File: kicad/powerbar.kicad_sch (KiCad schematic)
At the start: 24 parts, among them J31 Float 1, J32 Float 2, J33 Power bar 1, J34 Power bar 2, U10 PCA9685PW

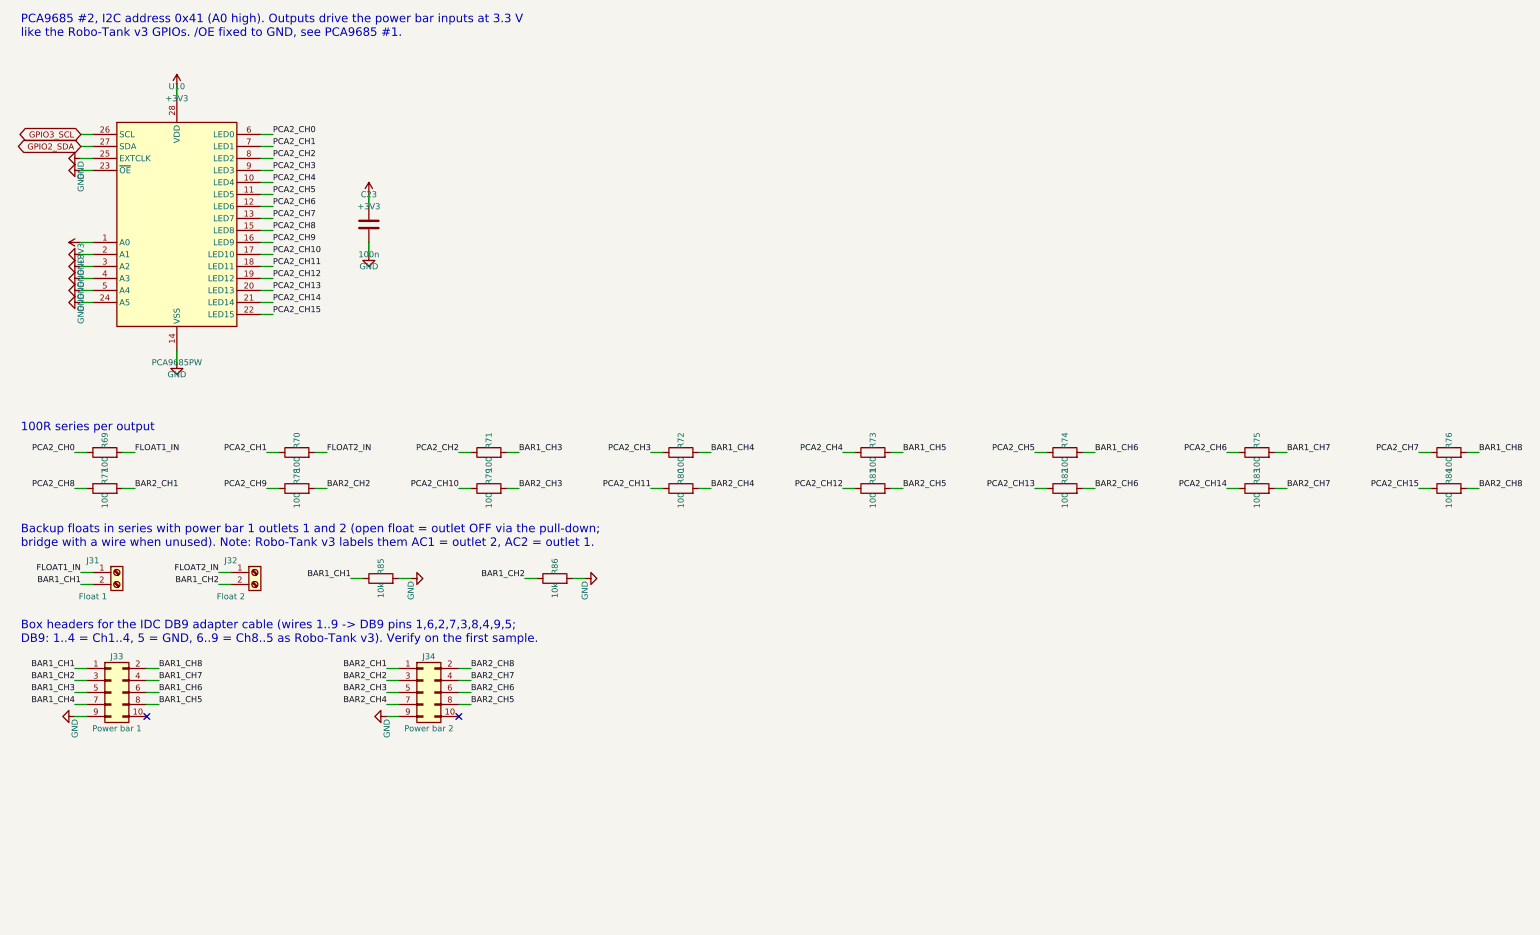
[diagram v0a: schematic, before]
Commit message: kicad: v2 space measures - feeder on power bar header, resistor arrays, 0603, TSSOP buffers
Feeder port dropped: power bar header pin 10 = +3V3_EXT (own AMS1117), any PCA #2 channel as signal; 30 series resistors as 8x 4x0603 arrays; new passives 0603; new 74HCT244 in TSSOP-20; flat parts may use the Pi zone, connectors anywhere else. ERC 0, DRC copper 0, parity 0.

Co-Authored-By: Claude Opus 5.5 <noreply@anthropic.com>
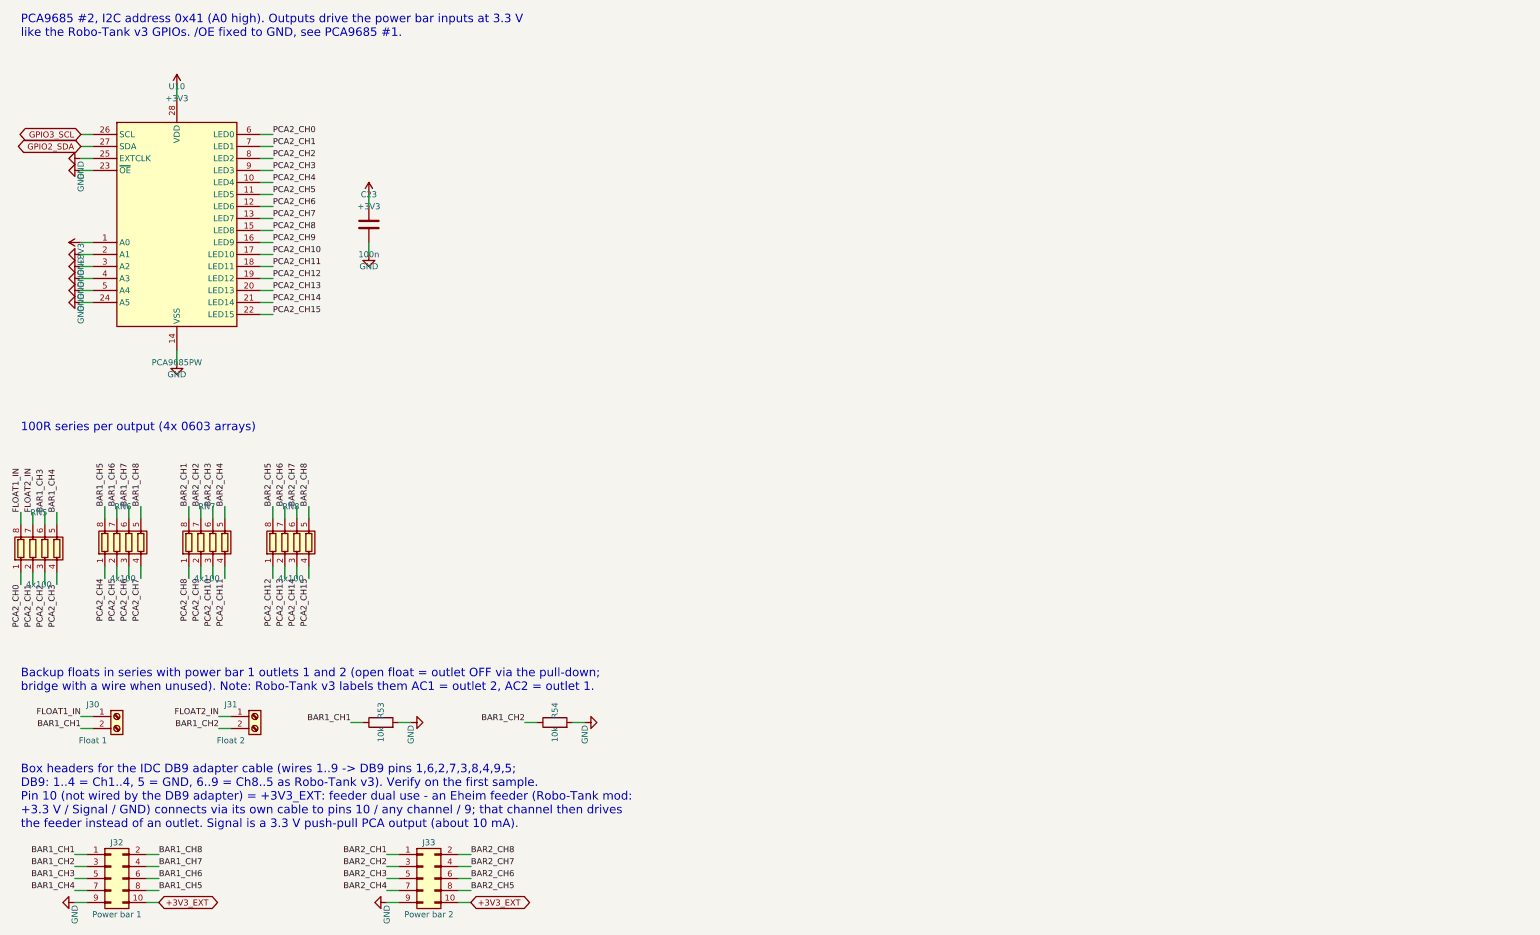
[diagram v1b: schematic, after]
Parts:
- removed J32: Float 2, aquaPCB:TerminalBlock_Kangnex_WJ250B-3.5-02P_P3.50mm_Staggered, symbol Connector:Screw_Terminal_01x02
- removed J34: Power bar 2, Connector_IDC:IDC-Header_2x05_P2.54mm_Vertical, symbol Connector_Generic:Conn_02x05_Odd_Even
- removed R69, R70, R71, R72, R73, R74, R75, R76, R77, R78, R79, R80, R81, R82, R83, R84: 100, Resistor_SMD:R_0805_2012Metric, symbol Device:R
- removed R85, R86: 10k, Resistor_SMD:R_0805_2012Metric, symbol Device:R
- added J30: Float 1, aquaPCB:TerminalBlock_Kangnex_WJ250B-3.5-02P_P3.50mm_Staggered, symbol Connector:Screw_Terminal_01x02
- added J32: Power bar 1, Connector_IDC:IDC-Header_2x05_P2.54mm_Vertical, symbol Connector_Generic:Conn_02x05_Odd_Even
- added R53, R54: 10k, Resistor_SMD:R_0603_1608Metric, symbol Device:R
- added RN5, RN6, RN7, RN8: 4x100, Resistor_SMD:R_Array_Convex_4x0603, symbol Device:R_Pack04
- C23: footprint Capacitor_SMD:C_0805_2012Metric -> Capacitor_SMD:C_0603_1608Metric; LCSC C49678 -> C14663
- J31: value Float 1 -> Float 2
- J33: value Power bar 1 -> Power bar 2
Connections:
- net BAR1_CH1: now also J30.2 (Pin_2), J32.1 (Pin_1), R53.1; no longer J31.2 (Pin_2), J33.1 (Pin_1)
- net BAR1_CH2: now also J31.2 (Pin_2), J32.3 (Pin_3), R54.1; no longer J33.3 (Pin_3)
- net BAR1_CH3: now also J32.5 (Pin_5), RN5.6 (R3.2); no longer J33.5 (Pin_5)
- net BAR1_CH4: now also J32.7 (Pin_7), RN5.5 (R4.2); no longer J33.7 (Pin_7)
- net BAR1_CH5: now also J32.8 (Pin_8), RN6.8 (R1.2); no longer J33.8 (Pin_8)
- net BAR1_CH6: now also J32.6 (Pin_6), RN6.7 (R2.2); no longer J33.6 (Pin_6)
- net BAR1_CH7: now also J32.4 (Pin_4), RN6.6 (R3.2); no longer J33.4 (Pin_4)
- net BAR1_CH8: now also J32.2 (Pin_2), RN6.5 (R4.2); no longer J33.2 (Pin_2)
- net BAR2_CH1: now also J33.1 (Pin_1), RN7.8 (R1.2)
- net BAR2_CH2: now also J33.3 (Pin_3), RN7.7 (R2.2)
- net BAR2_CH3: now also J33.5 (Pin_5), RN7.6 (R3.2)
- net BAR2_CH4: now also J33.7 (Pin_7), RN7.5 (R4.2)
- net BAR2_CH5: now also J33.8 (Pin_8), RN8.8 (R1.2)
- net BAR2_CH6: now also J33.6 (Pin_6), RN8.7 (R2.2)
- net BAR2_CH7: now also J33.4 (Pin_4), RN8.6 (R3.2)
- net BAR2_CH8: now also J33.2 (Pin_2), RN8.5 (R4.2)
- net FLOAT1_IN: now also J30.1 (Pin_1), RN5.8 (R1.2); no longer J31.1 (Pin_1)
- net FLOAT2_IN: now also J31.1 (Pin_1), RN5.7 (R2.2)
- net GND: now also J32.9 (Pin_9), R53.2, R54.2
- net PCA2_CH0: now also RN5.1 (R1.1)
- net PCA2_CH1: now also RN5.2 (R2.1)
- net PCA2_CH10: now also RN7.3 (R3.1)
- net PCA2_CH11: now also RN7.4 (R4.1)
- net PCA2_CH12: now also RN8.1 (R1.1)
- net PCA2_CH13: now also RN8.2 (R2.1)
- net PCA2_CH14: now also RN8.3 (R3.1)
- net PCA2_CH15: now also RN8.4 (R4.1)
- net PCA2_CH2: now also RN5.3 (R3.1)
- net PCA2_CH3: now also RN5.4 (R4.1)
- net PCA2_CH4: now also RN6.1 (R1.1)
- net PCA2_CH5: now also RN6.2 (R2.1)
- net PCA2_CH6: now also RN6.3 (R3.1)
- net PCA2_CH7: now also RN6.4 (R4.1)
- net PCA2_CH8: now also RN7.1 (R1.1)
- net PCA2_CH9: now also RN7.2 (R2.1)
- net +3V3_EXT: now reaches J33.10 (Pin_10)
- net +3V3_EXT: now also J32.10 (Pin_10)
- no-connect marks 2 -> 0
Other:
- note added: "100R series per output (4x 0603 arrays)"
- note added: "Box headers for the IDC DB9 adapter cable (wires 1..9 -> DB9 pins 1,6,2,7,3,8,4,9,5; DB9: 1..4 = Ch1..4, 5 = GND, 6..9 = Ch8..5 as Robo-Tank v3). Verify on the first sample. Pin 10 (not wired by the DB9 adapter) = +3V3_EXT: feeder dual use - an Eheim feeder (Robo-Tank mod: +3.3 V / Signal / GND) connects via its own cable to pins 10 / any channel / 9; that channel then drives the feeder instead o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"
- note removed: "100R series per output"
- note removed: "Box headers for the IDC DB9 adapter cable (wires 1..9 -> DB9 pins 1,6,2,7,3,8,4,9,5; DB9: 1..4 = Ch1..4, 5 = GND, 6..9 = Ch8..5 as Robo-Tank v3). Verify on the first sample."

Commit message: kicad: pin headers for 1-Wire, ADC and floats; connectivity-driven re-placement
J19, ADC sockets (J36/J37/J26/J27, 3x4 grid) and floats J30/J31 are pin headers now. All footprints placed on the board (big connectors first, flat parts allowed under the Pi, user-placed U10/RN5/J32/U11 and user routing kept): signal ratsnest 7824 -> 4450 mm, crossings 1776 -> 862. ERC 0, DRC copper 0, parity 0.

Co-Authored-By: Claude Opus 5.5 <noreply@anthropic.com>
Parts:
- J30, J31: footprint aquaPCB:TerminalBlock_Kangnex_WJ250B-3.5-02P_P3.50mm_Staggered -> Connector_PinHeader_2.54mm:PinHeader_1x02_P2.54mm_Vertical; symbol Connector:Screw_Terminal_01x02 -> Connector_Generic:Conn_01x02; LCSC C8454 -> (none)
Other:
- note removed: "100R series per output (4x 0603 arrays)"
- moved on the sheet: C23, RN5, RN6, RN7, RN8

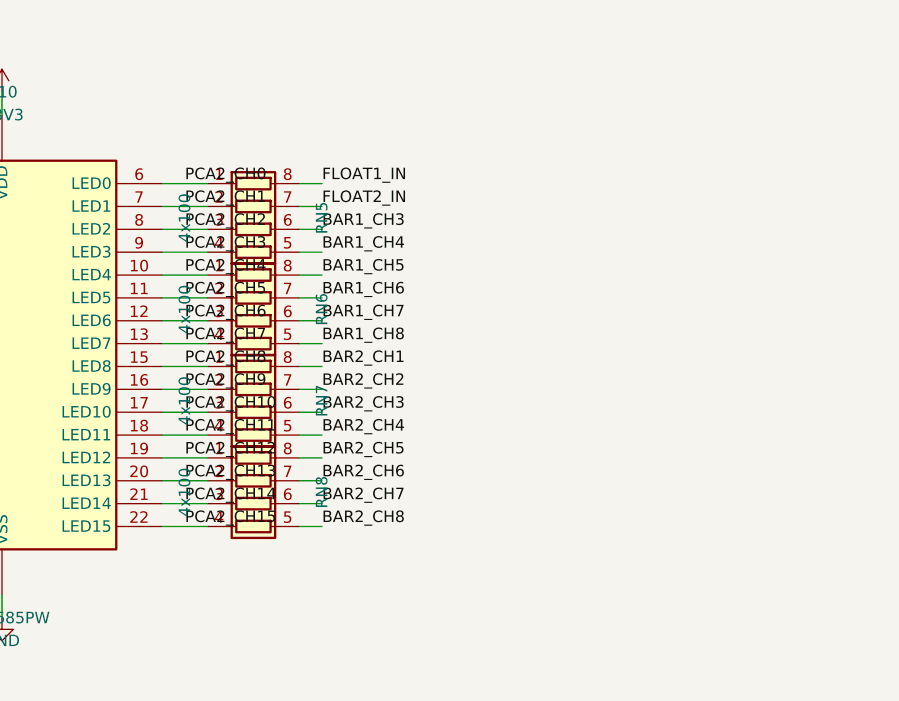
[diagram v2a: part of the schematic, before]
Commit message: kicad: power bar group re-placed and routed, 5 V I2C removed
- Power bars: U10 rotated, RN5..RN8 re-placed, J32/J33 rotated by 180 deg
  (pinout unchanged). Original PCA #2 channel order kept (bar 1 outlet n =
  ch n-1, bar 2 = ch n+7); identical array elements re-assigned in the
  schematic for routing. All power bar nets routed, U10 supply re-done,
  SDA/SCL escape stubs towards the Pi header.
- Sensors: 5 V I2C (PCA9306, J35) removed, I2C is 3.3 V only.
- Board: manual group placement and routing, Q4_DRV clearance fix,
  duplicate via and dangling GND stubs removed.
- README: 5 V I2C note and PCA #2 channel order / rotated headers.

Co-Authored-By: Claude Opus 5.5 <noreply@anthropic.com>
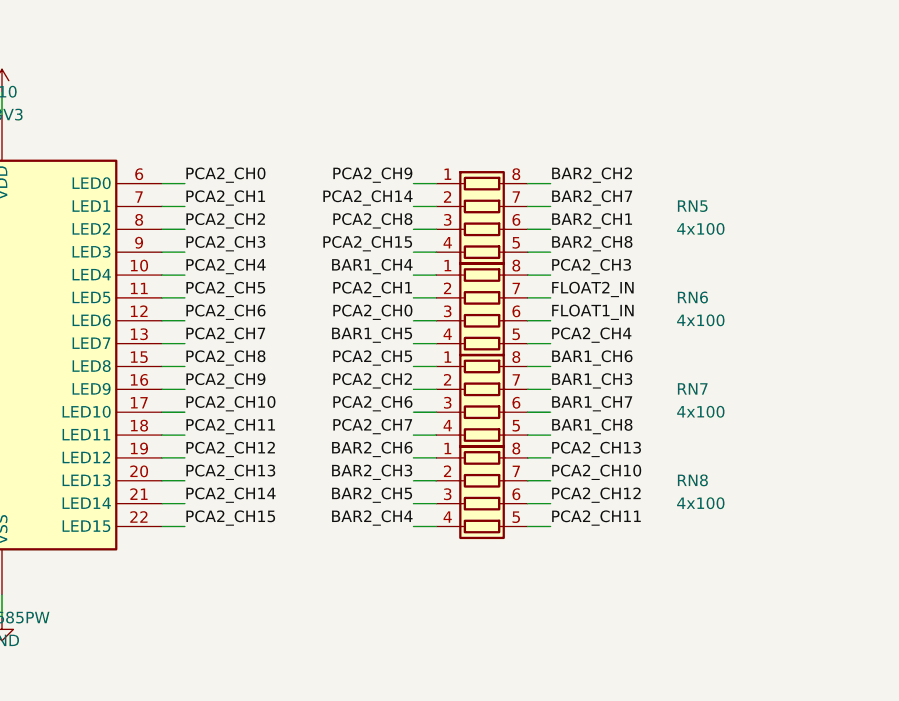
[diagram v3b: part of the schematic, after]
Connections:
- net BAR1_CH3: now also RN7.7 (R2.2); no longer RN5.6 (R3.2)
- net BAR1_CH4: now also RN6.1 (R1.1); no longer RN5.5 (R4.2)
- net BAR1_CH5: now also RN6.4 (R4.1); no longer RN6.8 (R1.2)
- net BAR1_CH6: now also RN7.8 (R1.2); no longer RN6.7 (R2.2)
- net BAR1_CH7: now also RN7.6 (R3.2); no longer RN6.6 (R3.2)
- net BAR1_CH8: now also RN7.5 (R4.2); no longer RN6.5 (R4.2)
- net BAR2_CH1: now also RN5.6 (R3.2); no longer RN7.8 (R1.2)
- net BAR2_CH2: now also RN5.8 (R1.2); no longer RN7.7 (R2.2)
- net BAR2_CH3: now also RN8.2 (R2.1); no longer RN7.6 (R3.2)
- net BAR2_CH4: now also RN8.4 (R4.1); no longer RN7.5 (R4.2)
- net BAR2_CH5: now also RN8.3 (R3.1); no longer RN8.8 (R1.2)
- net BAR2_CH6: now also RN8.1 (R1.1); no longer RN8.7 (R2.2)
- net BAR2_CH7: now also RN5.7 (R2.2); no longer RN8.6 (R3.2)
- net BAR2_CH8: now also RN5.5 (R4.2); no longer RN8.5 (R4.2)
- net FLOAT1_IN: now also RN6.6 (R3.2); no longer RN5.8 (R1.2)
- net FLOAT2_IN: now also RN6.7 (R2.2); no longer RN5.7 (R2.2)
- net PCA2_CH0: now also RN6.3 (R3.1); no longer RN5.1 (R1.1)
- net PCA2_CH1: now also RN6.2 (R2.1); no longer RN5.2 (R2.1)
- net PCA2_CH10: now also RN8.7 (R2.2); no longer RN7.3 (R3.1)
- net PCA2_CH11: now also RN8.5 (R4.2); no longer RN7.4 (R4.1)
- net PCA2_CH12: now also RN8.6 (R3.2); no longer RN8.1 (R1.1)
- net PCA2_CH13: now also RN8.8 (R1.2); no longer RN8.2 (R2.1)
- net PCA2_CH14: now also RN5.2 (R2.1); no longer RN8.3 (R3.1)
- net PCA2_CH15: now also RN5.4 (R4.1); no longer RN8.4 (R4.1)
- net PCA2_CH2: now also RN7.2 (R2.1); no longer RN5.3 (R3.1)
- net PCA2_CH3: now also RN6.8 (R1.2); no longer RN5.4 (R4.1)
- net PCA2_CH4: now also RN6.5 (R4.2); no longer RN6.1 (R1.1)
- net PCA2_CH5: now also RN7.1 (R1.1); no longer RN6.2 (R2.1)
- net PCA2_CH6: now also RN7.3 (R3.1); no longer RN6.3 (R3.1)
- net PCA2_CH7: now also RN7.4 (R4.1); no longer RN6.4 (R4.1)
- net PCA2_CH8: now also RN5.3 (R3.1); no longer RN7.1 (R1.1)
- net PCA2_CH9: now also RN5.1 (R1.1); no longer RN7.2 (R2.1)
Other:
- moved on the sheet: RN5, RN6, RN7, RN8

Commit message: kicad: v2 layout finished - ADC renumbering, port labels, last routes
- ADC sockets numbered 0..3 from right to left; AIN0<->AIN1 and AIN2<->AIN3
  swapped at the ADS1115, U5 end runs re-routed.
- Connector labels: IoRegistry-style port names (PCA#1 chNN, ADC #1 in n,
  GPIO n, DS1820); J5/J6/J8/J9 corrected from GPIO to PCA#1 ch15/14/13/12
  (also in outputs.kicad_sch). Back side: names with voltage/current
  ratings, running from the board edge at pin 1, "+" on supply pins,
  SCL/SDA and 1-Wire Data marks. Front: ADC #1 / in n, jumper labels.
- Routed the last six open nets (+3V3 at J24/JP4, +5V_EXT at J19,
  GPIO2_SDA J22-J23 on B.Cu, AIN1, J24 pin 10 - JP3, PCA1_CH1); PCA1_CH3
  partly moved to B.Cu to free the corridor at U7. Dangling stubs removed.
- Silkscreen: nothing on pads, overlaps reduced with small moves; part
  references and F.Fab texts at 0.8 mm.
- aquaPCB.kicad_dru: the deliberate courtyard overlap of the ADC socket
  pairs J26/J27 and J36/J37 (2.54 mm grid) is waived by a custom rule.

ERC clean, DRC without errors (silkscreen warnings only), board fully
routed and in sync with the schematic.

Co-Authored-By: Claude Opus 5.5 <noreply@anthropic.com>
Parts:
- C23: footprint Capacitor_SMD:C_0603_1608Metric -> Capacitor_SMD:C_0805_2012Metric; LCSC C14663 -> C49678
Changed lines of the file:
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@@
 			)
 		)
-		(property "Footprint" "Capacitor_SMD:C_0603_1608Metric"
+		(property "Footprint" "Capacitor_SMD:C_0805_2012Metric"
 			(at 168.91 80.01 0)
 			(hide yes)
@@
 			)
 		)
-		(property "LCSC" "C14663"
+		(property "LCSC" "C49678"
 			(at 168.91 80.01 0)
 			(hide yes)

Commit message: kicad: LCSC numbers for PCA9685 and PTC, status LED names follow PCA#1
- U7/U10 PCA9685PW,118 -> LCSC C2678753, F2 nSMD050 -> C69688 (schematic
  and board), so every assembled part carries an LCSC number.
- Status LEDs D9/D11/D15/D17 renamed GPIO12/13/16/26 -> PCA#1 ch15/14/13/12,
  matching the Q2/Q3/Q5/Q6 drive since v2.

Co-Authored-By: Claude Opus 5.5 <noreply@anthropic.com>
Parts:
- U10: LCSC (none) -> C2678753
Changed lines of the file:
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@@
+			)
+		)
+		(property "LCSC" "C2678753"
+			(at 58.42 73.66 0)
+			(hide yes)
+			(show_name no)
+			(do_not_autoplace no)
+			(effects
+				(font
+					(size 1.27 1.27)
+				)
 			)
 		)
